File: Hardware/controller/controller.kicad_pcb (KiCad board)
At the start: 4 copper layers, 128.1 x 184.5 mm, 116 parts, among them J101 Conn_02x10_Odd_Even, J102 Conn_02x10_Odd_Even, J103 Conn_02x10_Odd_Even, J301 Conn_ARM_JTAG_SWD_10, J302 Conn_01x03_Male, M101 Fan_4pin, Q101 MMBT3904, Q301 MMBT3904, SW301 B3F-1005, SW302 B3F-1002, SW303 228ADS2AAWFCMBA, U101 PCA9543A, U102 EMC2101-R, U201 BD9C301FJ, U302 ATSAME51J20A-A, U303 AT25SF321B-SSHB, U401 KSZ8041TL, X401 50MHz, Y301 32.768kHz, Y302 12MHz

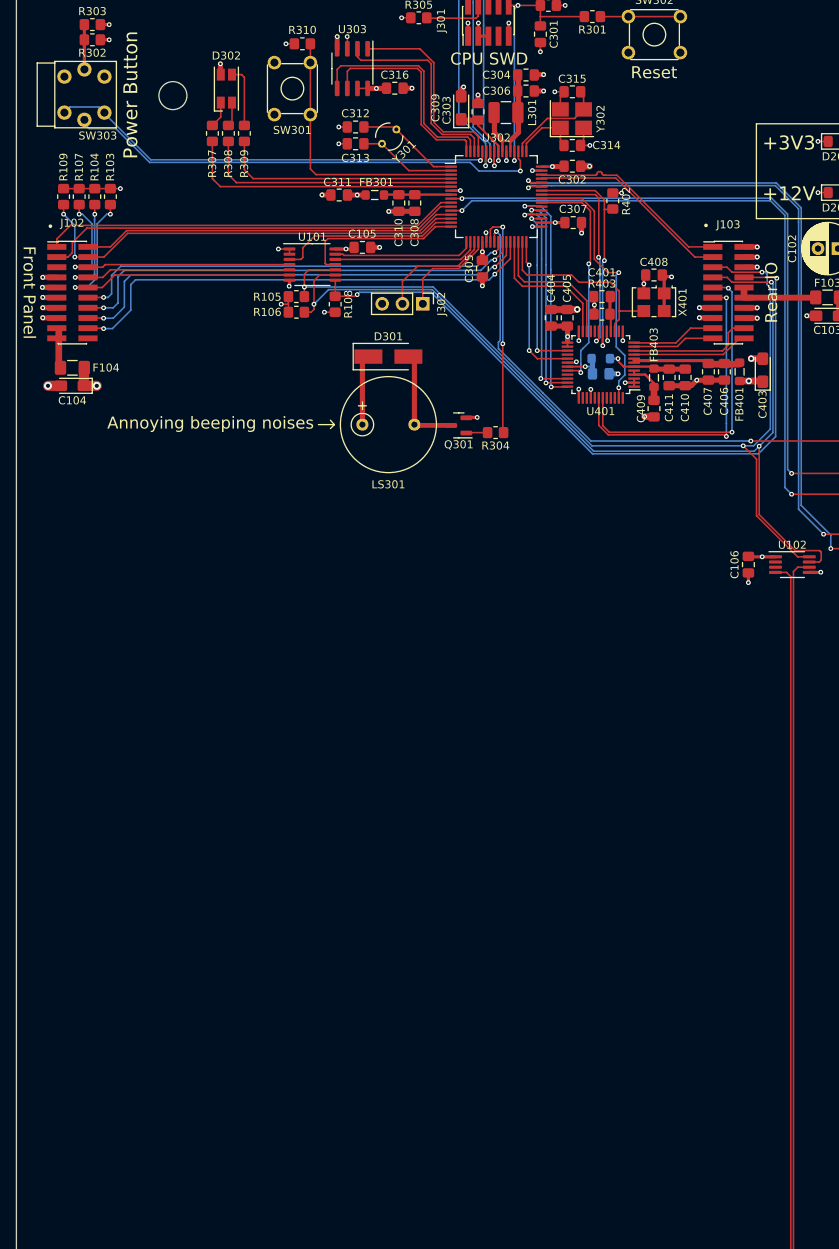
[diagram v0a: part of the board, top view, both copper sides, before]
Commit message: More tweaks to controller board
- Moved a few components around to make more space for cables from front
  panel jacks; namely, the beeper and front panel connector were moved
  somewhat and traces cleaned up
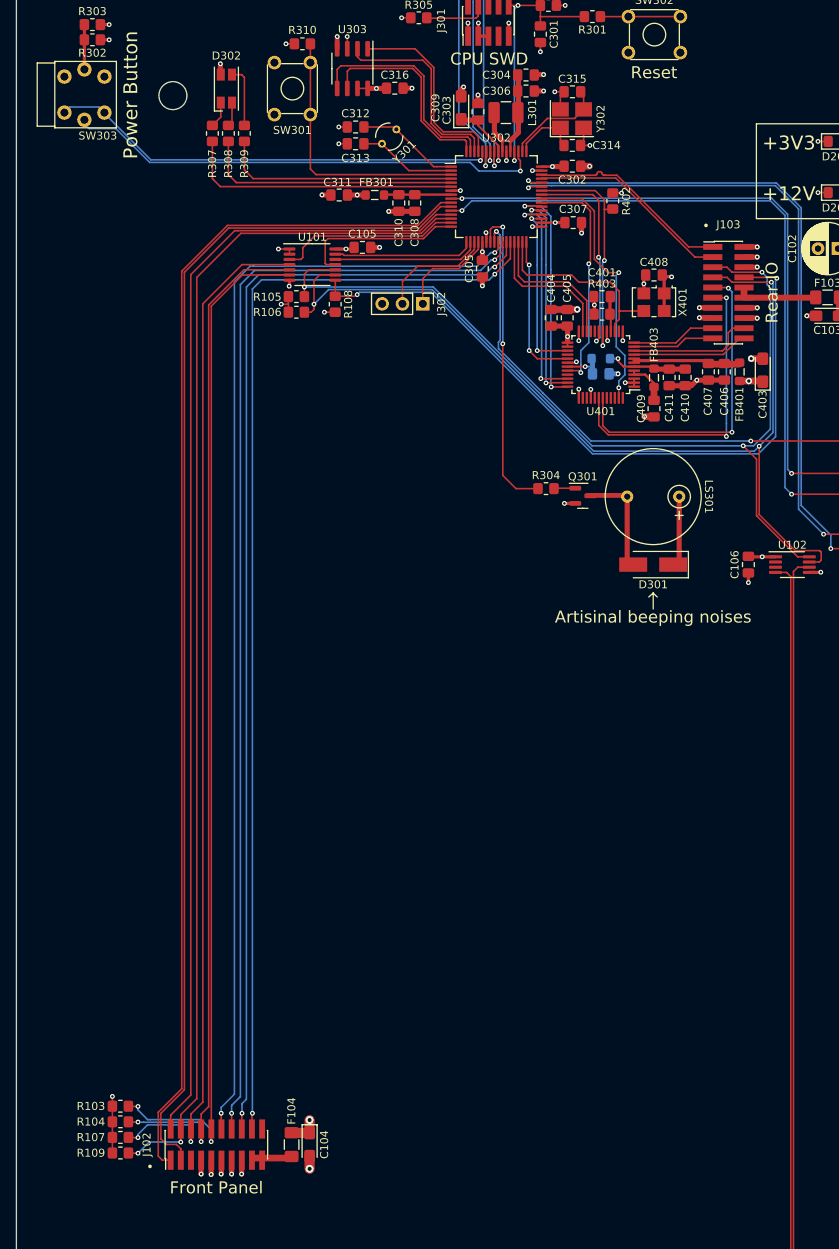
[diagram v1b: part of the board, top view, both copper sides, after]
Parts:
- moved R109 119.8 mm to (33.0, 167.6), turned to 180 degrees
- moved R107 117.7 mm to (33.0, 165.6), turned to 180 degrees
- moved R104 115.7 mm to (33.0, 163.7), turned to 180 degrees
- moved R103 113.7 mm to (33.0, 161.7), turned to 180 degrees
- moved J102 108.0 mm to (45.0, 166.5), turned to 90 degrees
- moved F104 100.9 mm to (54.4, 166.5), turned to 90 degrees
- moved C104 99.4 mm to (56.6, 166.5), turned to -90 degrees
- moved D301 42.1 mm to (99.6, 94.0), turned to 180 degrees
- moved LS301 34.3 mm to (99.6, 85.5), turned to 180 degrees
- moved Q301 17.8 mm to (90.8, 85.4), turned to 0 degrees
- moved R304 9.42 mm to (86.2, 84.5), turned to 0 degrees
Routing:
- net /FRONT_ENC_A: track 52.2 -> 150.8 mm
- net /FRONT_ENC_B: track 52.6 -> 150.7 mm
- net /DISP_D/~{C}: track 47.1 -> 143.5 mm
- net /~{FRONT_RESET}: track 56.2 -> 150.9 mm
- net /~{FRONT_IRQ}: track 37.5 -> 128.8 mm
- net /FRONT_SDA: track 38.5 -> 128.2 mm
- net /FRONT_SCL: track 40.8 -> 129.1 mm
- net /DISP_MISO: track 56.1 -> 142.2 mm
- net /DISP_SCK: track 57.9 -> 141.7 mm
- net /~{DISP_CS}: track 59.1 -> 141.3 mm
- net /DISP_MOSI: track 60.4 -> 140.9 mm
- net /CPU/BEEPER: track 29.4 -> 39.4 mm
- net /CPU/NOR_SCK: track 26.0 -> 25.4 mm
- net /CPU/NOR_MOSI: track 28.3 -> 27.7 mm
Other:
- board text added: "Artisinal beeping noises"
- board text removed: "Annoying beeping noises"

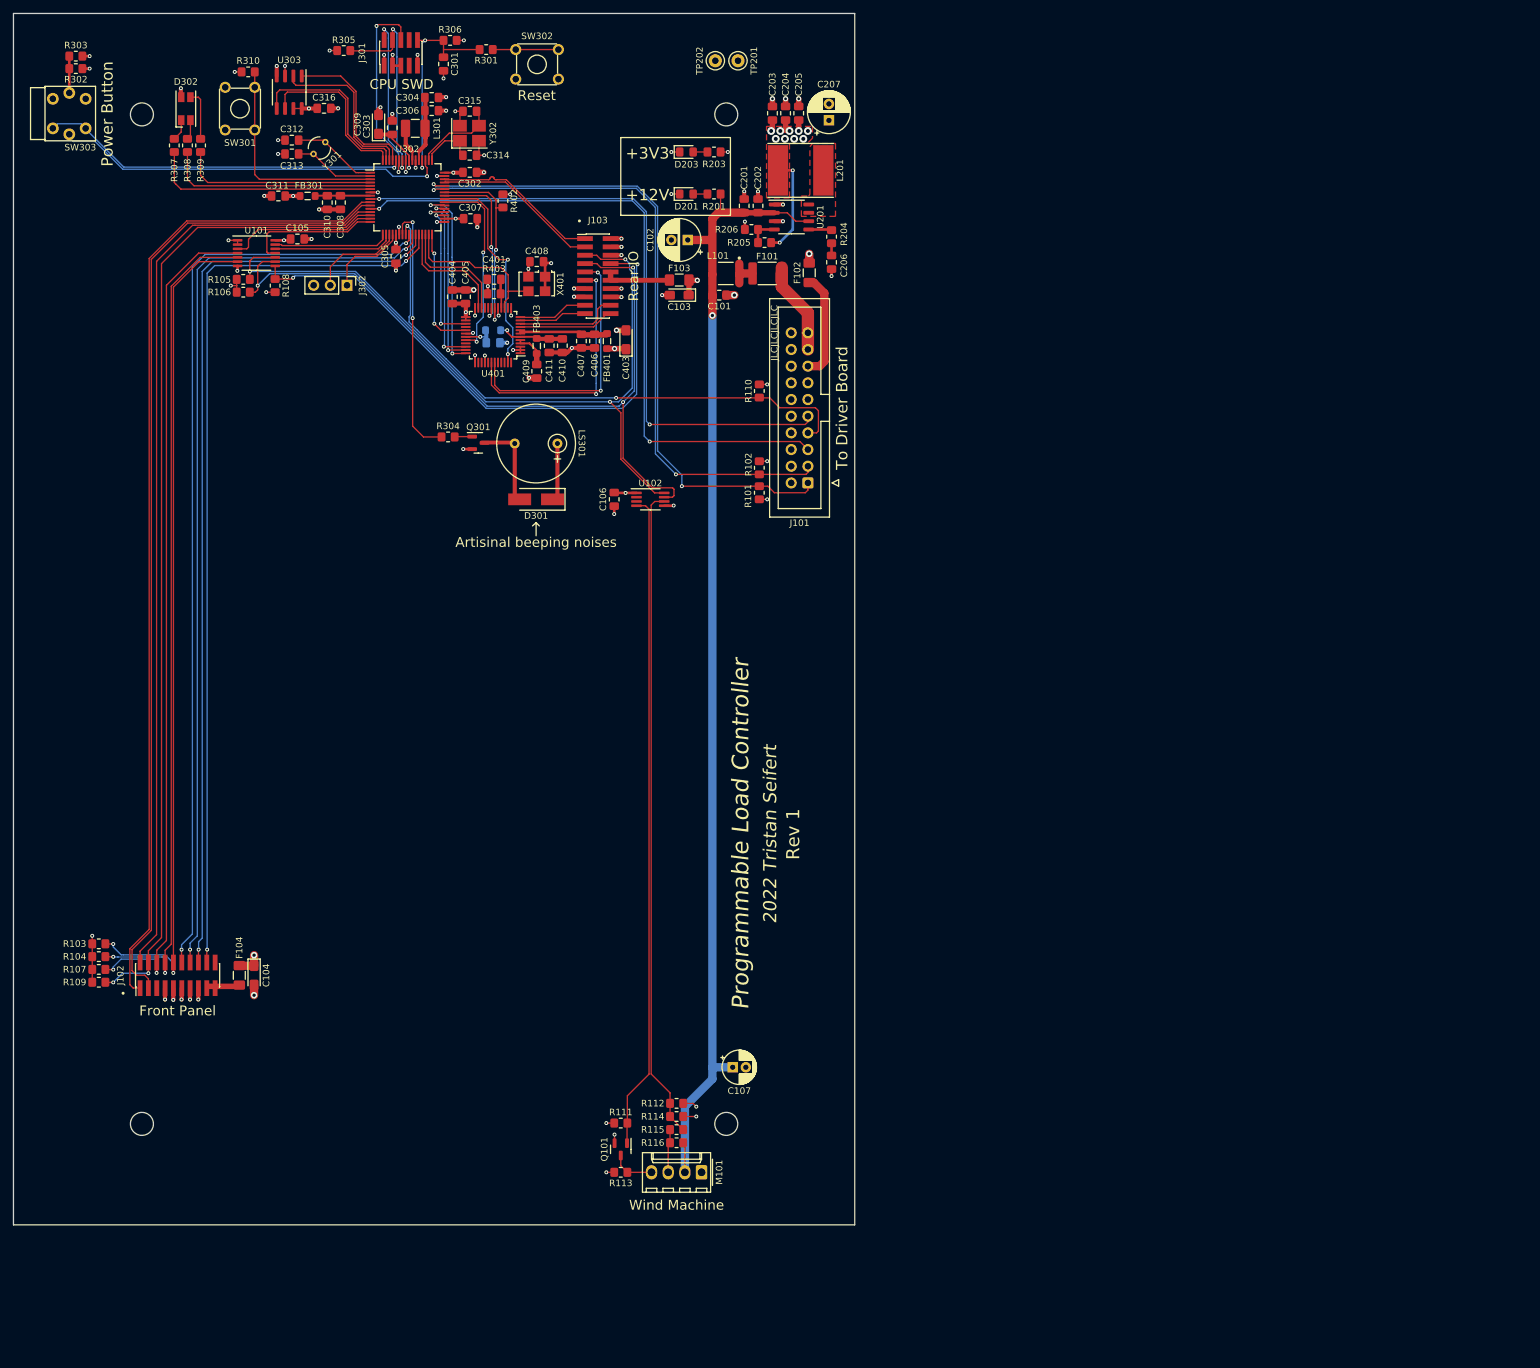
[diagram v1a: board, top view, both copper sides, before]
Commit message: Driver input protection; heatsink footprint tweaks
- Updated the footprint for the heatsink on the driver board to include
  a 3D model. Also fixed it… the distances were kind of out of whack and
  it would never have really fit

- Added a reverse polarity protection diode to the input; it gets its
  own cute little heatsink

- Minor movement to better accomodate a fan. A 20mm fan will likely
  interfere with the input connector (it might be worth switching to a
  different kind, or just soldering the connections altogether: spade
  terminals seem like a good choice for high current) and be very tight
  against the input diode's heatsink. We'll try with a 10mm fan and see
  if that's enough airflow.
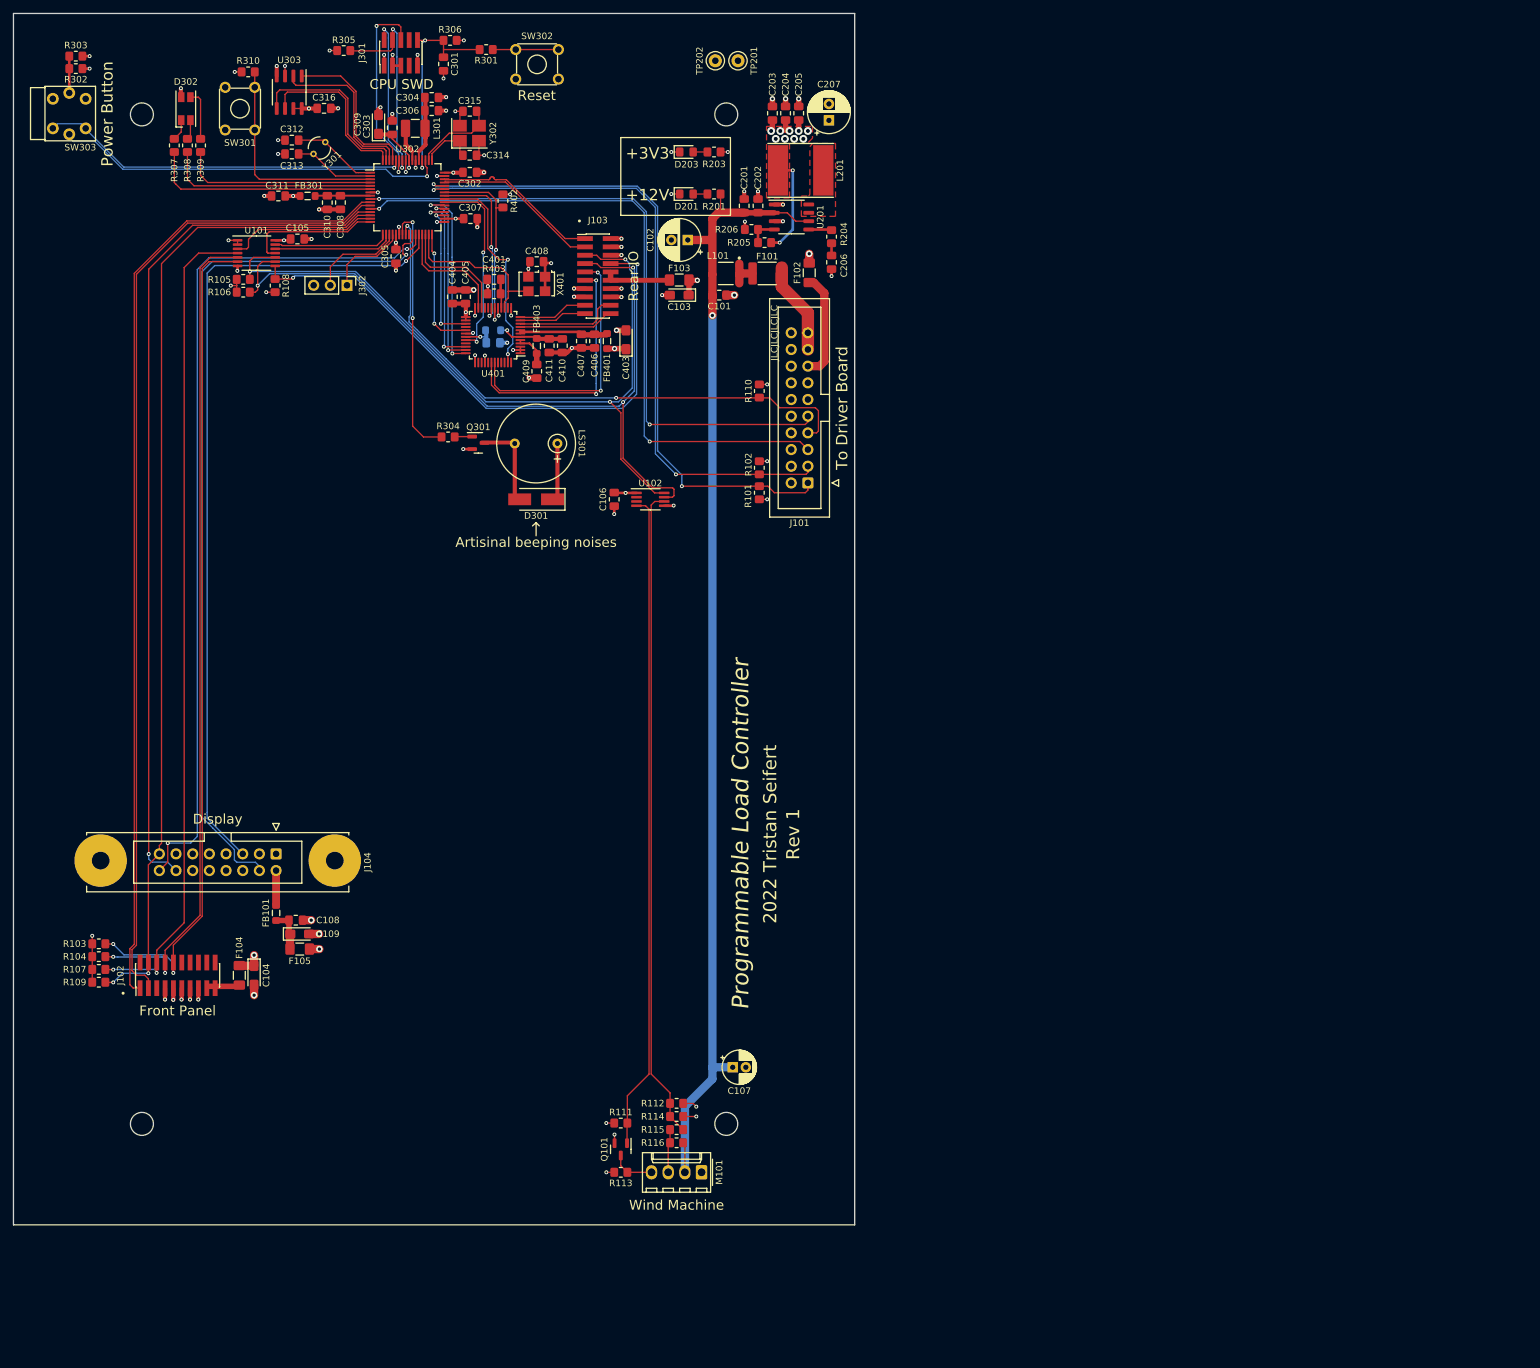
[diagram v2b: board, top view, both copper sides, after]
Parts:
- added C108: 100nF, Capacitor_SMD:C_0805_2012Metric_Pad1.18x1.45mm_HandSolder, F.Cu at (63.0, 158.1)
- added C109: 10µF, Capacitor_Tantalum_SMD:CP_EIA-3216-18_Kemet-A_Pad1.58x1.35mm_HandSolder, F.Cu at (63.6, 160.2)
- added F105: 500mA, Fuse:Fuse_1206_3216Metric_Pad1.42x1.75mm_HandSolder, F.Cu at (63.6, 162.5)
- added FB101: FerriteBead_Small, Inductor_SMD:L_0805_2012Metric_Pad1.05x1.20mm_HandSolder, F.Cu at (60.0, 157.0)
- added J104: Conn_02x08_Odd_Even, Connector_IDC:IDC-Header_2x08-1MP_P2.54mm_Latch_Vertical, F.Cu at (60.0, 148.0)
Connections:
- J102 pad 12: /DISP_MISO -> unconnected-(J102-Pad12)
- J102 pad 14: /DISP_SCK -> unconnected-(J102-Pad14)
- J102 pad 16: /~{DISP_CS} -> unconnected-(J102-Pad16)
- J102 pad 18: /DISP_MOSI -> unconnected-(J102-Pad18)
- J102 pad 2: /DISP_D/~{C} -> unconnected-(J102-Pad2)
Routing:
- net /DISP_MISO: track 142.2 -> 0.00 mm, vias 2 -> 0
- net /DISP_MOSI: track 140.9 -> 126.6 mm, vias 2 -> 1
- net /DISP_D/~{C}: track 143.5 -> 132.1 mm, vias 0 -> 1
- net /~{DISP_CS}: track 141.3 -> 132.3 mm
- net /DISP_SCK: track 141.7 -> 133.2 mm, vias 2 -> 1
- net Net-(C108-Pad2): track 0.00 -> 6.06 mm
- net Net-(FB101-Pad2): track 0.00 -> 5.16 mm
- net GND: track 112.9 -> 115.7 mm, vias 71 -> 73
- net /~{FRONT_IRQ}: track 128.8 -> 126.4 mm
- net +3V3: track 110.5 -> 112.0 mm, vias 44 -> 45
- net /FRONT_SCL: track 129.1 -> 128.0 mm
- net /FRONT_SDA: track 128.2 -> 127.3 mm
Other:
- board text added: "Display"
